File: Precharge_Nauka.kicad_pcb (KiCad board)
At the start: 2 copper layers, 80 parts, among them Q1 2N7002, Q2 C2M0280120D, Q3 C2M0280120D, Q4 C2M0280120D, Q5 C2M0280120D, U1 LM2903, U2 LMV321IDBVR, U3 74LVC1G08, U4 LMV321IDBVR

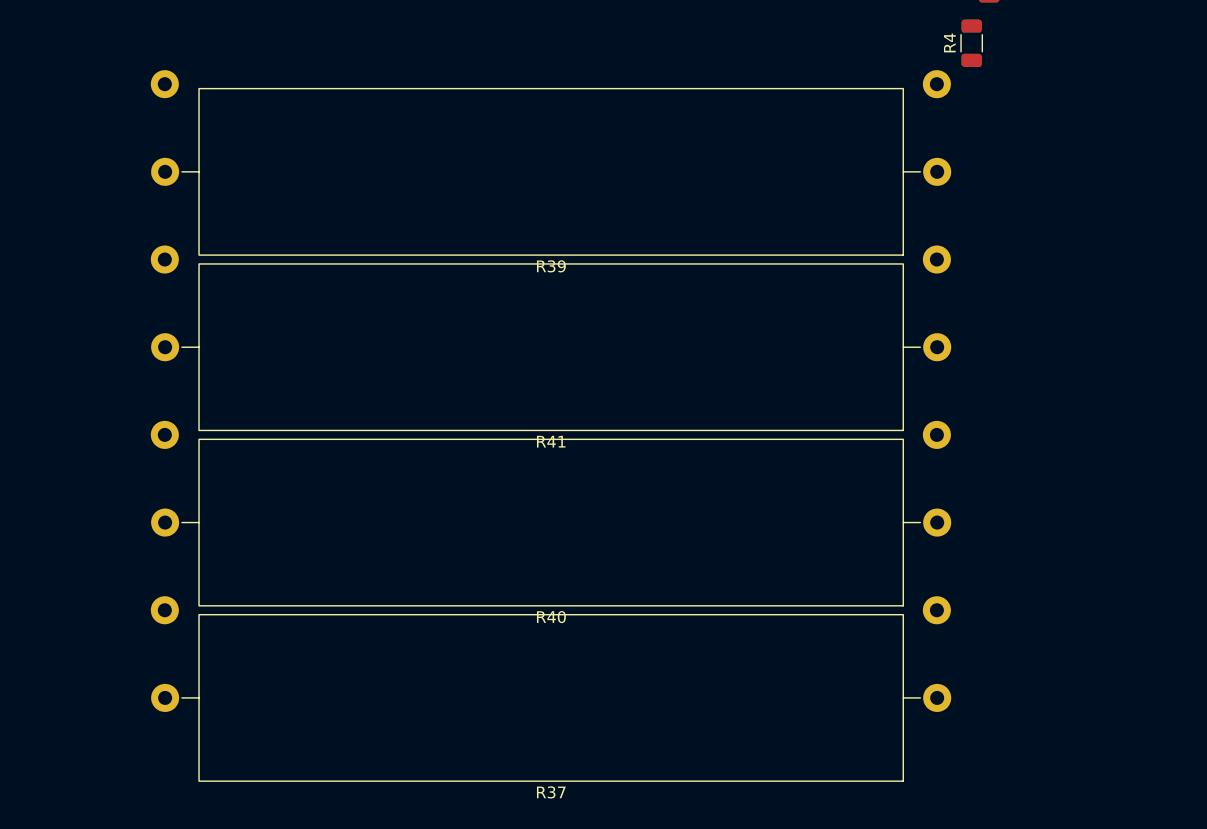
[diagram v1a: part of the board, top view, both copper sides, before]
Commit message: VER1.0: заменил цементные на 2512 резисторы
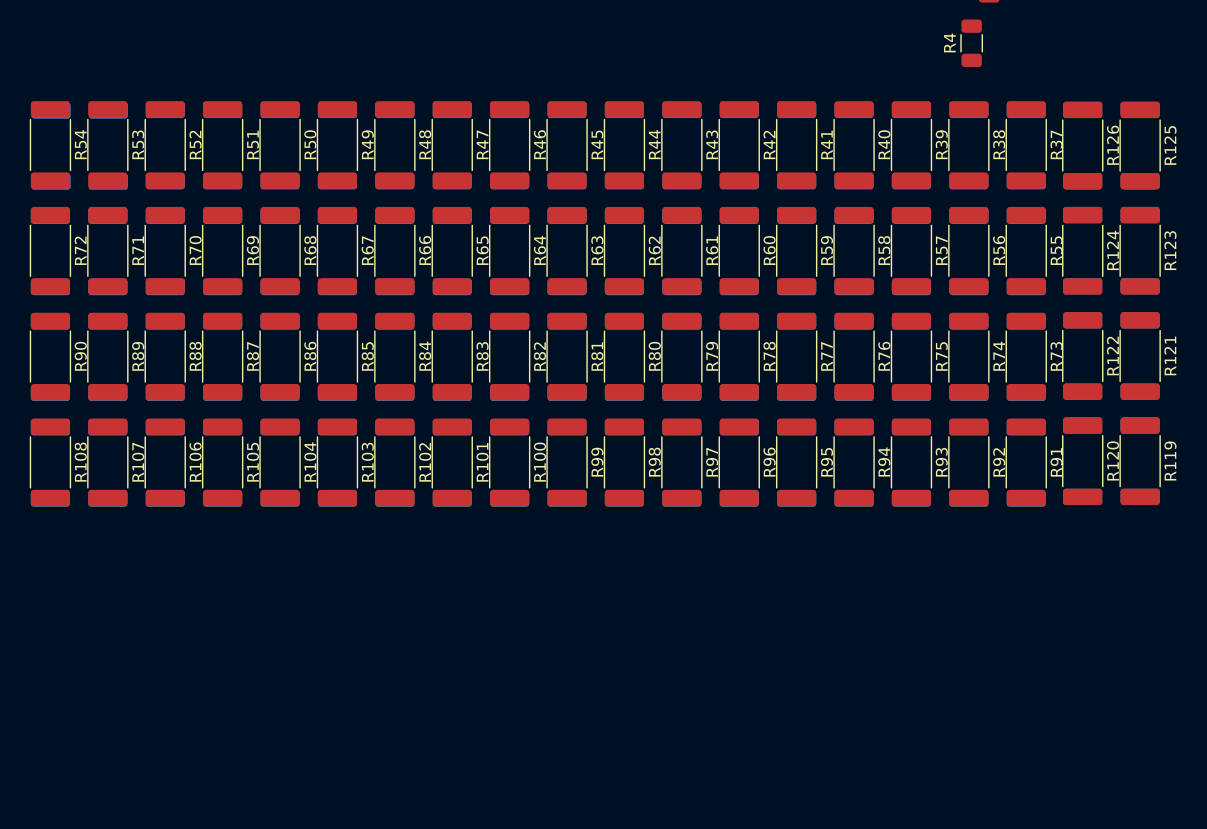
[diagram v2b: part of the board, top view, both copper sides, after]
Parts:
- added R100: 15, Resistor_SMD:R_2512_6332Metric_Pad1.40x3.35mm_HandSolder, F.Cu at (182.5, 224.6)
- added R101: 15, Resistor_SMD:R_2512_6332Metric_Pad1.40x3.35mm_HandSolder, F.Cu at (177.6, 224.6)
- added R102: 15, Resistor_SMD:R_2512_6332Metric_Pad1.40x3.35mm_HandSolder, F.Cu at (172.7, 224.6)
- added R103: 15, Resistor_SMD:R_2512_6332Metric_Pad1.40x3.35mm_HandSolder, F.Cu at (167.8, 224.6)
- added R104: 15, Resistor_SMD:R_2512_6332Metric_Pad1.40x3.35mm_HandSolder, F.Cu at (162.8, 224.6)
- added R105: 15, Resistor_SMD:R_2512_6332Metric_Pad1.40x3.35mm_HandSolder, F.Cu at (157.9, 224.6)
- added R106: 15, Resistor_SMD:R_2512_6332Metric_Pad1.40x3.35mm_HandSolder, F.Cu at (153.0, 224.6)
- added R107: 15, Resistor_SMD:R_2512_6332Metric_Pad1.40x3.35mm_HandSolder, F.Cu at (148.1, 224.6)
- added R108: 15, Resistor_SMD:R_2512_6332Metric_Pad1.40x3.35mm_HandSolder, F.Cu at (143.2, 224.6)
- added R109: 15, Resistor_SMD:R_2512_6332Metric_Pad1.40x3.35mm_HandSolder, B.Cu at (148.2, 197.6)
- added R110: 15, Resistor_SMD:R_2512_6332Metric_Pad1.40x3.35mm_HandSolder, B.Cu at (143.2, 197.6)
- added R111: 15, Resistor_SMD:R_2512_6332Metric_Pad1.40x3.35mm_HandSolder, B.Cu at (236.4, 197.5)
- added R112: 15, Resistor_SMD:R_2512_6332Metric_Pad1.40x3.35mm_HandSolder, B.Cu at (231.5, 197.5)
- added R113: 15, Resistor_SMD:R_2512_6332Metric_Pad1.40x3.35mm_HandSolder, B.Cu at (236.4, 206.5)
- added R114: 15, Resistor_SMD:R_2512_6332Metric_Pad1.40x3.35mm_HandSolder, B.Cu at (231.5, 206.5)
- added R115: 15, Resistor_SMD:R_2512_6332Metric_Pad1.40x3.35mm_HandSolder, B.Cu at (236.4, 215.5)
- added R116: 15, Resistor_SMD:R_2512_6332Metric_Pad1.40x3.35mm_HandSolder, B.Cu at (231.5, 215.5)
- added R117: 15, Resistor_SMD:R_2512_6332Metric_Pad1.40x3.35mm_HandSolder, B.Cu at (236.4, 224.5)
- added R118: 15, Resistor_SMD:R_2512_6332Metric_Pad1.40x3.35mm_HandSolder, B.Cu at (231.5, 224.5)
- added R119: 15, Resistor_SMD:R_2512_6332Metric_Pad1.40x3.35mm_HandSolder, F.Cu at (236.4, 224.5)
- added R120: 15, Resistor_SMD:R_2512_6332Metric_Pad1.40x3.35mm_HandSolder, F.Cu at (231.5, 224.5)
- added R121: 15, Resistor_SMD:R_2512_6332Metric_Pad1.40x3.35mm_HandSolder, F.Cu at (236.4, 215.5)
- added R122: 15, Resistor_SMD:R_2512_6332Metric_Pad1.40x3.35mm_HandSolder, F.Cu at (231.5, 215.5)
- added R123: 15, Resistor_SMD:R_2512_6332Metric_Pad1.40x3.35mm_HandSolder, F.Cu at (236.4, 206.5)
- added R124: 15, Resistor_SMD:R_2512_6332Metric_Pad1.40x3.35mm_HandSolder, F.Cu at (231.5, 206.5)
- added R125: 15, Resistor_SMD:R_2512_6332Metric_Pad1.40x3.35mm_HandSolder, F.Cu at (236.4, 197.5)
- added R126: 15, Resistor_SMD:R_2512_6332Metric_Pad1.40x3.35mm_HandSolder, F.Cu at (231.5, 197.5)
- added R127: 15, Resistor_SMD:R_2512_6332Metric_Pad1.40x3.35mm_HandSolder, B.Cu at (226.7, 224.7)
- added R128: 15, Resistor_SMD:R_2512_6332Metric_Pad1.40x3.35mm_HandSolder, B.Cu at (221.8, 224.7)
- added R129: 15, Resistor_SMD:R_2512_6332Metric_Pad1.40x3.35mm_HandSolder, B.Cu at (216.8, 224.7)
- added R130: 15, Resistor_SMD:R_2512_6332Metric_Pad1.40x3.35mm_HandSolder, B.Cu at (211.9, 224.7)
- added R131: 15, Resistor_SMD:R_2512_6332Metric_Pad1.40x3.35mm_HandSolder, B.Cu at (207.0, 224.7)
- added R132: 15, Resistor_SMD:R_2512_6332Metric_Pad1.40x3.35mm_HandSolder, B.Cu at (202.1, 224.7)
- added R133: 15, Resistor_SMD:R_2512_6332Metric_Pad1.40x3.35mm_HandSolder, B.Cu at (197.2, 224.7)
- added R134: 15, Resistor_SMD:R_2512_6332Metric_Pad1.40x3.35mm_HandSolder, B.Cu at (192.3, 224.7)
- added R135: 15, Resistor_SMD:R_2512_6332Metric_Pad1.40x3.35mm_HandSolder, B.Cu at (187.4, 224.7)
- added R136: 15, Resistor_SMD:R_2512_6332Metric_Pad1.40x3.35mm_HandSolder, B.Cu at (182.5, 224.7)
- added R137: 15, Resistor_SMD:R_2512_6332Metric_Pad1.40x3.35mm_HandSolder, B.Cu at (177.6, 224.7)
- added R138: 15, Resistor_SMD:R_2512_6332Metric_Pad1.40x3.35mm_HandSolder, B.Cu at (172.7, 224.7)
- added R139: 15, Resistor_SMD:R_2512_6332Metric_Pad1.40x3.35mm_HandSolder, B.Cu at (167.8, 224.7)
- added R140: 15, Resistor_SMD:R_2512_6332Metric_Pad1.40x3.35mm_HandSolder, B.Cu at (162.8, 224.7)
- added R141: 15, Resistor_SMD:R_2512_6332Metric_Pad1.40x3.35mm_HandSolder, B.Cu at (157.9, 224.7)
- added R142: 15, Resistor_SMD:R_2512_6332Metric_Pad1.40x3.35mm_HandSolder, B.Cu at (153.0, 224.7)
- added R143: 15, Resistor_SMD:R_2512_6332Metric_Pad1.40x3.35mm_HandSolder, B.Cu at (148.1, 224.7)
- added R144: 15, Resistor_SMD:R_2512_6332Metric_Pad1.40x3.35mm_HandSolder, B.Cu at (143.2, 224.7)
- added R145: 15, Resistor_SMD:R_2512_6332Metric_Pad1.40x3.35mm_HandSolder, B.Cu at (226.7, 215.6)
- added R146: 15, Resistor_SMD:R_2512_6332Metric_Pad1.40x3.35mm_HandSolder, B.Cu at (221.8, 215.6)
- added R147: 15, Resistor_SMD:R_2512_6332Metric_Pad1.40x3.35mm_HandSolder, B.Cu at (216.8, 215.6)
- added R148: 15, Resistor_SMD:R_2512_6332Metric_Pad1.40x3.35mm_HandSolder, B.Cu at (211.9, 215.6)
- added R149: 15, Resistor_SMD:R_2512_6332Metric_Pad1.40x3.35mm_HandSolder, B.Cu at (207.0, 215.6)
- added R150: 15, Resistor_SMD:R_2512_6332Metric_Pad1.40x3.35mm_HandSolder, B.Cu at (202.1, 215.6)
- added R151: 15, Resistor_SMD:R_2512_6332Metric_Pad1.40x3.35mm_HandSolder, B.Cu at (197.2, 215.6)
- added R152: 15, Resistor_SMD:R_2512_6332Metric_Pad1.40x3.35mm_HandSolder, B.Cu at (192.3, 215.6)
- added R153: 15, Resistor_SMD:R_2512_6332Metric_Pad1.40x3.35mm_HandSolder, B.Cu at (187.4, 215.6)
- added R154: 15, Resistor_SMD:R_2512_6332Metric_Pad1.40x3.35mm_HandSolder, B.Cu at (182.5, 215.6)
- added R155: 15, Resistor_SMD:R_2512_6332Metric_Pad1.40x3.35mm_HandSolder, B.Cu at (177.6, 215.6)
- added R156: 15, Resistor_SMD:R_2512_6332Metric_Pad1.40x3.35mm_HandSolder, B.Cu at (172.7, 215.6)
- added R157: 15, Resistor_SMD:R_2512_6332Metric_Pad1.40x3.35mm_HandSolder, B.Cu at (167.8, 215.6)
- added R158: 15, Resistor_SMD:R_2512_6332Metric_Pad1.40x3.35mm_HandSolder, B.Cu at (162.8, 215.6)
- added R159: 15, Resistor_SMD:R_2512_6332Metric_Pad1.40x3.35mm_HandSolder, B.Cu at (157.9, 215.6)
- added R160: 15, Resistor_SMD:R_2512_6332Metric_Pad1.40x3.35mm_HandSolder, B.Cu at (153.0, 215.6)
- added R161: 15, Resistor_SMD:R_2512_6332Metric_Pad1.40x3.35mm_HandSolder, B.Cu at (148.1, 215.6)
- added R162: 15, Resistor_SMD:R_2512_6332Metric_Pad1.40x3.35mm_HandSolder, B.Cu at (143.2, 215.6)
- added R163: 15, Resistor_SMD:R_2512_6332Metric_Pad1.40x3.35mm_HandSolder, B.Cu at (226.7, 206.6)
- added R164: 15, Resistor_SMD:R_2512_6332Metric_Pad1.40x3.35mm_HandSolder, B.Cu at (221.8, 206.6)
- added R165: 15, Resistor_SMD:R_2512_6332Metric_Pad1.40x3.35mm_HandSolder, B.Cu at (216.8, 206.6)
- added R166: 15, Resistor_SMD:R_2512_6332Metric_Pad1.40x3.35mm_HandSolder, B.Cu at (211.9, 206.6)
- added R167: 15, Resistor_SMD:R_2512_6332Metric_Pad1.40x3.35mm_HandSolder, B.Cu at (207.0, 206.6)
- added R168: 15, Resistor_SMD:R_2512_6332Metric_Pad1.40x3.35mm_HandSolder, B.Cu at (202.1, 206.6)
- added R169: 15, Resistor_SMD:R_2512_6332Metric_Pad1.40x3.35mm_HandSolder, B.Cu at (197.2, 206.6)
- added R170: 15, Resistor_SMD:R_2512_6332Metric_Pad1.40x3.35mm_HandSolder, B.Cu at (192.3, 206.6)
- added R171: 15, Resistor_SMD:R_2512_6332Metric_Pad1.40x3.35mm_HandSolder, B.Cu at (187.4, 206.6)
- added R172: 15, Resistor_SMD:R_2512_6332Metric_Pad1.40x3.35mm_HandSolder, B.Cu at (182.5, 206.6)
- added R173: 15, Resistor_SMD:R_2512_6332Metric_Pad1.40x3.35mm_HandSolder, B.Cu at (177.6, 206.6)
- added R174: 15, Resistor_SMD:R_2512_6332Metric_Pad1.40x3.35mm_HandSolder, B.Cu at (172.7, 206.6)
- added R175: 15, Resistor_SMD:R_2512_6332Metric_Pad1.40x3.35mm_HandSolder, B.Cu at (167.8, 206.6)
- added R176: 15, Resistor_SMD:R_2512_6332Metric_Pad1.40x3.35mm_HandSolder, B.Cu at (162.8, 206.6)
- added R177: 15, Resistor_SMD:R_2512_6332Metric_Pad1.40x3.35mm_HandSolder, B.Cu at (157.9, 206.6)
- added R178: 15, Resistor_SMD:R_2512_6332Metric_Pad1.40x3.35mm_HandSolder, B.Cu at (153.0, 206.6)
- added R179: 15, Resistor_SMD:R_2512_6332Metric_Pad1.40x3.35mm_HandSolder, B.Cu at (148.1, 206.6)
- added R180: 15, Resistor_SMD:R_2512_6332Metric_Pad1.40x3.35mm_HandSolder, B.Cu at (143.2, 206.6)
- added R181: 15, Resistor_SMD:R_2512_6332Metric_Pad1.40x3.35mm_HandSolder, B.Cu at (226.7, 197.5)
- added R182: 15, Resistor_SMD:R_2512_6332Metric_Pad1.40x3.35mm_HandSolder, B.Cu at (221.8, 197.5)
- added R183: 15, Resistor_SMD:R_2512_6332Metric_Pad1.40x3.35mm_HandSolder, B.Cu at (216.8, 197.5)
- added R184: 15, Resistor_SMD:R_2512_6332Metric_Pad1.40x3.35mm_HandSolder, B.Cu at (211.9, 197.5)
- added R185: 15, Resistor_SMD:R_2512_6332Metric_Pad1.40x3.35mm_HandSolder, B.Cu at (207.0, 197.5)
- added R186: 15, Resistor_SMD:R_2512_6332Metric_Pad1.40x3.35mm_HandSolder, B.Cu at (202.1, 197.5)
- added R187: 15, Resistor_SMD:R_2512_6332Metric_Pad1.40x3.35mm_HandSolder, B.Cu at (197.2, 197.5)
- added R188: 15, Resistor_SMD:R_2512_6332Metric_Pad1.40x3.35mm_HandSolder, B.Cu at (192.3, 197.5)
- added R189: 15, Resistor_SMD:R_2512_6332Metric_Pad1.40x3.35mm_HandSolder, B.Cu at (187.4, 197.5)
- added R190: 15, Resistor_SMD:R_2512_6332Metric_Pad1.40x3.35mm_HandSolder, B.Cu at (182.5, 197.5)
- added R191: 15, Resistor_SMD:R_2512_6332Metric_Pad1.40x3.35mm_HandSolder, B.Cu at (177.6, 197.5)
- added R192: 15, Resistor_SMD:R_2512_6332Metric_Pad1.40x3.35mm_HandSolder, B.Cu at (172.7, 197.5)
- added R193: 15, Resistor_SMD:R_2512_6332Metric_Pad1.40x3.35mm_HandSolder, B.Cu at (167.8, 197.5)
- added R194: 15, Resistor_SMD:R_2512_6332Metric_Pad1.40x3.35mm_HandSolder, B.Cu at (162.8, 197.5)
- added R195: 15, Resistor_SMD:R_2512_6332Metric_Pad1.40x3.35mm_HandSolder, B.Cu at (157.9, 197.5)
- added R196: 15, Resistor_SMD:R_2512_6332Metric_Pad1.40x3.35mm_HandSolder, B.Cu at (153.0, 197.5)
- added R45: 15, Resistor_SMD:R_2512_6332Metric_Pad1.40x3.35mm_HandSolder, F.Cu at (187.4, 197.4)
- added R46: 15, Resistor_SMD:R_2512_6332Metric_Pad1.40x3.35mm_HandSolder, F.Cu at (182.5, 197.4)
- added R47: 15, Resistor_SMD:R_2512_6332Metric_Pad1.40x3.35mm_HandSolder, F.Cu at (177.6, 197.4)
- added R48: 15, Resistor_SMD:R_2512_6332Metric_Pad1.40x3.35mm_HandSolder, F.Cu at (172.7, 197.4)
- added R49: 15, Resistor_SMD:R_2512_6332Metric_Pad1.40x3.35mm_HandSolder, F.Cu at (167.8, 197.4)
- added R50: 15, Resistor_SMD:R_2512_6332Metric_Pad1.40x3.35mm_HandSolder, F.Cu at (162.8, 197.4)
- added R51: 15, Resistor_SMD:R_2512_6332Metric_Pad1.40x3.35mm_HandSolder, F.Cu at (157.9, 197.4)
- added R52: 15, Resistor_SMD:R_2512_6332Metric_Pad1.40x3.35mm_HandSolder, F.Cu at (153.0, 197.4)
- added R53: 15, Resistor_SMD:R_2512_6332Metric_Pad1.40x3.35mm_HandSolder, F.Cu at (148.1, 197.4)
- added R54: 15, Resistor_SMD:R_2512_6332Metric_Pad1.40x3.35mm_HandSolder, F.Cu at (143.2, 197.4)
- added R55: 15, Resistor_SMD:R_2512_6332Metric_Pad1.40x3.35mm_HandSolder, F.Cu at (226.7, 206.5)
- added R56: 15, Resistor_SMD:R_2512_6332Metric_Pad1.40x3.35mm_HandSolder, F.Cu at (221.8, 206.5)
- added R57: 15, Resistor_SMD:R_2512_6332Metric_Pad1.40x3.35mm_HandSolder, F.Cu at (216.8, 206.5)
- added R58: 15, Resistor_SMD:R_2512_6332Metric_Pad1.40x3.35mm_HandSolder, F.Cu at (211.9, 206.5)
- added R59: 15, Resistor_SMD:R_2512_6332Metric_Pad1.40x3.35mm_HandSolder, F.Cu at (207.0, 206.5)
- added R60: 15, Resistor_SMD:R_2512_6332Metric_Pad1.40x3.35mm_HandSolder, F.Cu at (202.1, 206.5)
- added R61: 15, Resistor_SMD:R_2512_6332Metric_Pad1.40x3.35mm_HandSolder, F.Cu at (197.2, 206.5)
- added R62: 15, Resistor_SMD:R_2512_6332Metric_Pad1.40x3.35mm_HandSolder, F.Cu at (192.3, 206.5)
- added R63: 15, Resistor_SMD:R_2512_6332Metric_Pad1.40x3.35mm_HandSolder, F.Cu at (187.4, 206.5)
- added R64: 15, Resistor_SMD:R_2512_6332Metric_Pad1.40x3.35mm_HandSolder, F.Cu at (182.5, 206.5)
- added R65: 15, Resistor_SMD:R_2512_6332Metric_Pad1.40x3.35mm_HandSolder, F.Cu at (177.6, 206.5)
- added R66: 15, Resistor_SMD:R_2512_6332Metric_Pad1.40x3.35mm_HandSolder, F.Cu at (172.7, 206.5)
- added R67: 15, Resistor_SMD:R_2512_6332Metric_Pad1.40x3.35mm_HandSolder, F.Cu at (167.8, 206.5)
- added R68: 15, Resistor_SMD:R_2512_6332Metric_Pad1.40x3.35mm_HandSolder, F.Cu at (162.8, 206.5)
- added R69: 15, Resistor_SMD:R_2512_6332Metric_Pad1.40x3.35mm_HandSolder, F.Cu at (157.9, 206.5)
- added R70: 15, Resistor_SMD:R_2512_6332Metric_Pad1.40x3.35mm_HandSolder, F.Cu at (153.0, 206.5)
- added R71: 15, Resistor_SMD:R_2512_6332Metric_Pad1.40x3.35mm_HandSolder, F.Cu at (148.1, 206.5)
- added R72: 15, Resistor_SMD:R_2512_6332Metric_Pad1.40x3.35mm_HandSolder, F.Cu at (143.2, 206.5)
- added R73: 15, Resistor_SMD:R_2512_6332Metric_Pad1.40x3.35mm_HandSolder, F.Cu at (226.7, 215.6)
- added R74: 15, Resistor_SMD:R_2512_6332Metric_Pad1.40x3.35mm_HandSolder, F.Cu at (221.8, 215.6)
- added R75: 15, Resistor_SMD:R_2512_6332Metric_Pad1.40x3.35mm_HandSolder, F.Cu at (216.8, 215.6)
- added R76: 15, Resistor_SMD:R_2512_6332Metric_Pad1.40x3.35mm_HandSolder, F.Cu at (211.9, 215.6)
- added R77: 15, Resistor_SMD:R_2512_6332Metric_Pad1.40x3.35mm_HandSolder, F.Cu at (207.0, 215.6)
- added R78: 15, Resistor_SMD:R_2512_6332Metric_Pad1.40x3.35mm_HandSolder, F.Cu at (202.1, 215.6)
- added R79: 15, Resistor_SMD:R_2512_6332Metric_Pad1.40x3.35mm_HandSolder, F.Cu at (197.2, 215.6)
- added R80: 15, Resistor_SMD:R_2512_6332Metric_Pad1.40x3.35mm_HandSolder, F.Cu at (192.3, 215.6)
- added R81: 15, Resistor_SMD:R_2512_6332Metric_Pad1.40x3.35mm_HandSolder, F.Cu at (187.4, 215.6)
- added R82: 15, Resistor_SMD:R_2512_6332Metric_Pad1.40x3.35mm_HandSolder, F.Cu at (182.5, 215.6)
- added R83: 15, Resistor_SMD:R_2512_6332Metric_Pad1.40x3.35mm_HandSolder, F.Cu at (177.6, 215.6)
- added R84: 15, Resistor_SMD:R_2512_6332Metric_Pad1.40x3.35mm_HandSolder, F.Cu at (172.7, 215.6)
- added R85: 15, Resistor_SMD:R_2512_6332Metric_Pad1.40x3.35mm_HandSolder, F.Cu at (167.8, 215.6)
- added R86: 15, Resistor_SMD:R_2512_6332Metric_Pad1.40x3.35mm_HandSolder, F.Cu at (162.8, 215.6)
- added R87: 15, Resistor_SMD:R_2512_6332Metric_Pad1.40x3.35mm_HandSolder, F.Cu at (157.9, 215.6)
- added R88: 15, Resistor_SMD:R_2512_6332Metric_Pad1.40x3.35mm_HandSolder, F.Cu at (153.0, 215.6)
- added R89: 15, Resistor_SMD:R_2512_6332Metric_Pad1.40x3.35mm_HandSolder, F.Cu at (148.1, 215.6)
- added R90: 15, Resistor_SMD:R_2512_6332Metric_Pad1.40x3.35mm_HandSolder, F.Cu at (143.2, 215.6)
- added R91: 15, Resistor_SMD:R_2512_6332Metric_Pad1.40x3.35mm_HandSolder, F.Cu at (226.7, 224.6)
- added R92: 15, Resistor_SMD:R_2512_6332Metric_Pad1.40x3.35mm_HandSolder, F.Cu at (221.8, 224.6)
- added R93: 15, Resistor_SMD:R_2512_6332Metric_Pad1.40x3.35mm_HandSolder, F.Cu at (216.8, 224.6)
- added R94: 15, Resistor_SMD:R_2512_6332Metric_Pad1.40x3.35mm_HandSolder, F.Cu at (211.9, 224.6)
- added R95: 15, Resistor_SMD:R_2512_6332Metric_Pad1.40x3.35mm_HandSolder, F.Cu at (207.0, 224.6)
- added R96: 15, Resistor_SMD:R_2512_6332Metric_Pad1.40x3.35mm_HandSolder, F.Cu at (202.1, 224.6)
- added R97: 15, Resistor_SMD:R_2512_6332Metric_Pad1.40x3.35mm_HandSolder, F.Cu at (197.2, 224.6)
- added R98: 15, Resistor_SMD:R_2512_6332Metric_Pad1.40x3.35mm_HandSolder, F.Cu at (192.3, 224.6)
- added R99: 15, Resistor_SMD:R_2512_6332Metric_Pad1.40x3.35mm_HandSolder, F.Cu at (187.4, 224.6)
- C10: value 1u -> 100n
- R37, R39, R40, R41: value 10k -> 15; footprint Resistor_THT:R_Axial_Power_L60.0mm_W14.0mm_P66.04mm -> Resistor_SMD:R_2512_6332Metric_Pad1.40x3.35mm_HandSolder
- R38, R42, R43, R44: value 10k -> 15; footprint Resistor_THT:R_Axial_Power_L60.0mm_W14.0mm_P66.04mm -> Resistor_SMD:R_2512_6332Metric_Pad1.40x3.35mm_HandSolder; moved to F.Cu
- moved R37 47.9 mm to (226.7, 197.4), turned to -90 degrees
- moved R38 39.9 mm to (221.8, 197.4), turned to -90 degrees
- moved R44 36.5 mm to (192.3, 197.4), turned to -90 degrees
- moved R40 33.1 mm to (211.9, 197.4), turned to -90 degrees
- moved R43 22.4 mm to (197.2, 197.4), turned to -90 degrees
- moved R41 21.1 mm to (207.0, 197.4), turned to -90 degrees
- moved R42 19.5 mm to (202.1, 197.4), turned to -90 degrees
- moved R39 3.18 mm to (216.8, 197.4), turned to -90 degrees
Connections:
- R37 pad 1: VDC_IN -> VDC_OUT
- R37 pad 2: VDC_OUT -> VDC_IN
- R38 pad 1: VDC_IN -> VDC_OUT
- R38 pad 2: VDC_OUT -> VDC_IN
- R39 pad 1: VDC_IN -> VDC_OUT
- R39 pad 2: VDC_OUT -> VDC_IN
- R40 pad 1: VDC_IN -> VDC_OUT
- R40 pad 2: VDC_OUT -> VDC_IN
- R41 pad 1: VDC_IN -> VDC_OUT
- R41 pad 2: VDC_OUT -> VDC_IN
- R42 pad 1: VDC_IN -> VDC_OUT
- R42 pad 2: VDC_OUT -> VDC_IN
- R43 pad 1: VDC_IN -> VDC_OUT
- R43 pad 2: VDC_OUT -> VDC_IN
- R44 pad 1: VDC_IN -> VDC_OUT
- R44 pad 2: VDC_OUT -> VDC_IN

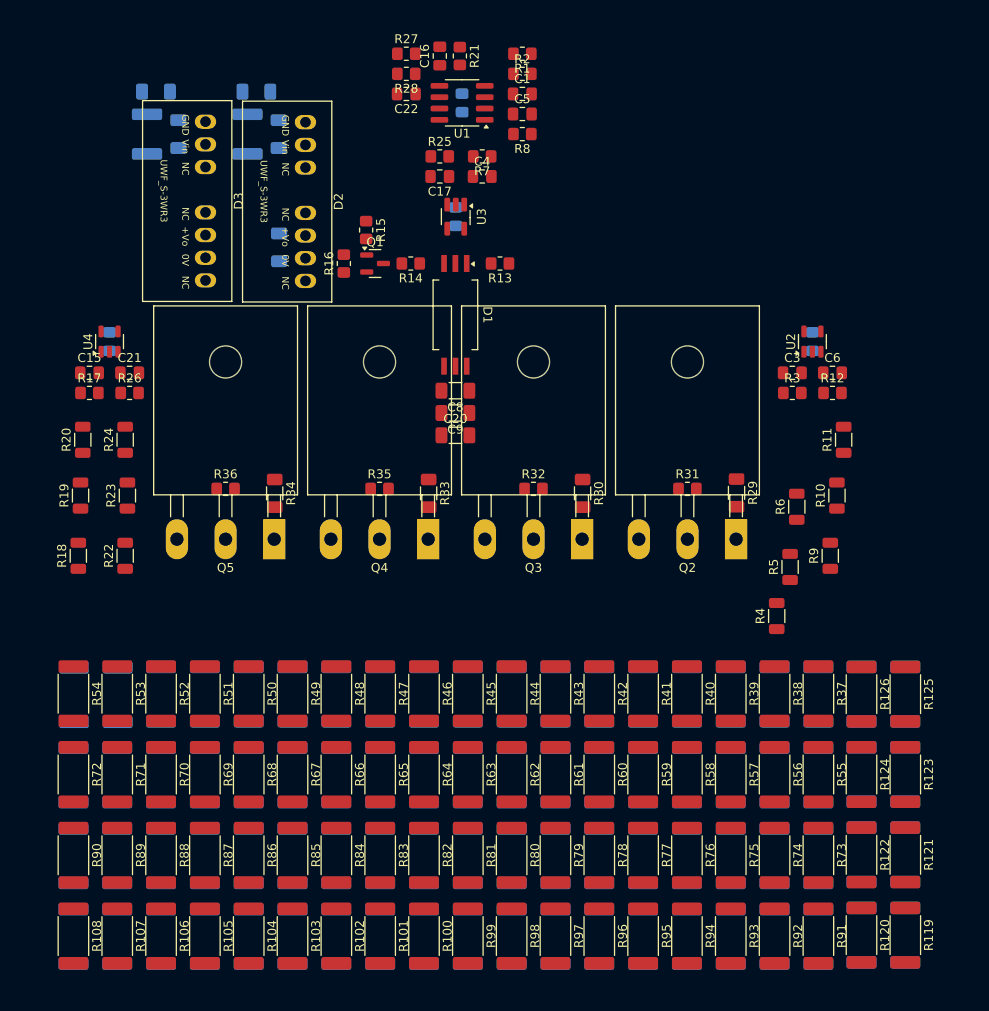
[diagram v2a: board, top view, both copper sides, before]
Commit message: VER1.0: надо проверить посадку новых транзисторов. Добавил обратную свзязь для компараторов
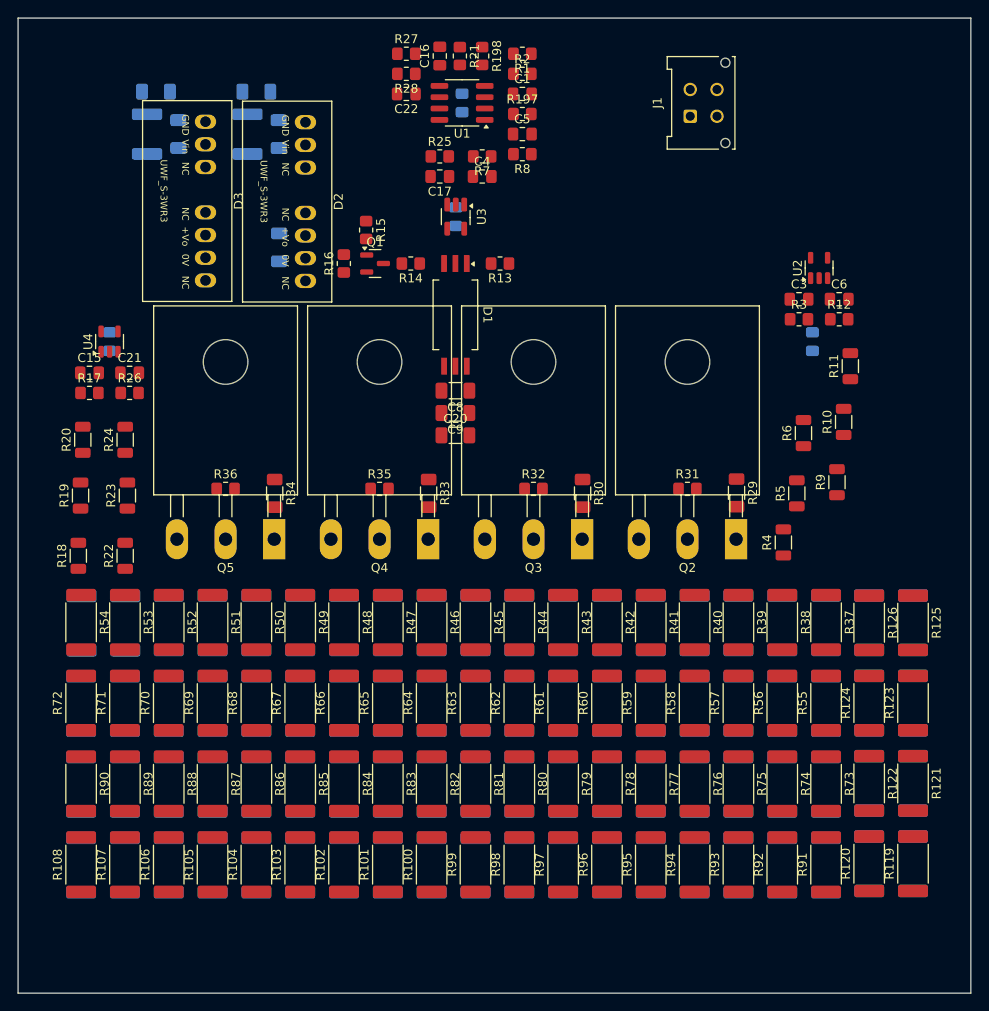
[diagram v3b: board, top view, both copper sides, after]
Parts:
- added J1: Conn_02x02_Top_Bottom, Connector_Molex:Molex_Micro-Fit_3.0_43045-0412_2x02_P3.00mm_Vertical, F.Cu at (212.3, 132.8)
- added R197: 10k, Resistor_SMD:R_0805_2012Metric_Pad1.20x1.40mm_HandSolder, F.Cu at (193.5, 132.5)
- added R198: 10k, Resistor_SMD:R_0805_2012Metric_Pad1.20x1.40mm_HandSolder, F.Cu at (189.0, 126.0)
- D1: value ~ -> NSI6801
- moved C3 8.28 mm to (224.5, 153.2)
- moved C6 8.28 mm to (229.0, 153.2)
- moved R10 8.28 mm to (229.5, 167.0)
- moved R11 8.28 mm to (230.2, 160.8)
- moved R12 8.28 mm to (229.0, 155.5)
- moved R3 8.28 mm to (224.5, 155.5)
- moved R4 8.28 mm to (222.8, 180.5)
- moved R5 8.28 mm to (224.2, 175.0)
- moved R6 8.28 mm to (225.0, 168.2)
- moved R9 8.28 mm to (228.8, 173.8)
- moved U2 8.28 mm to (226.8, 149.8)
- moved R100 8.05 mm to (183.3, 216.6), turned to 90 degrees
- moved R101 8.05 mm to (178.4, 216.6), turned to 90 degrees
- moved R102 8.05 mm to (173.5, 216.6), turned to 90 degrees
- moved R103 8.05 mm to (168.6, 216.6), turned to 90 degrees
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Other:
- board outline added: 106.8 x 109.2 mm

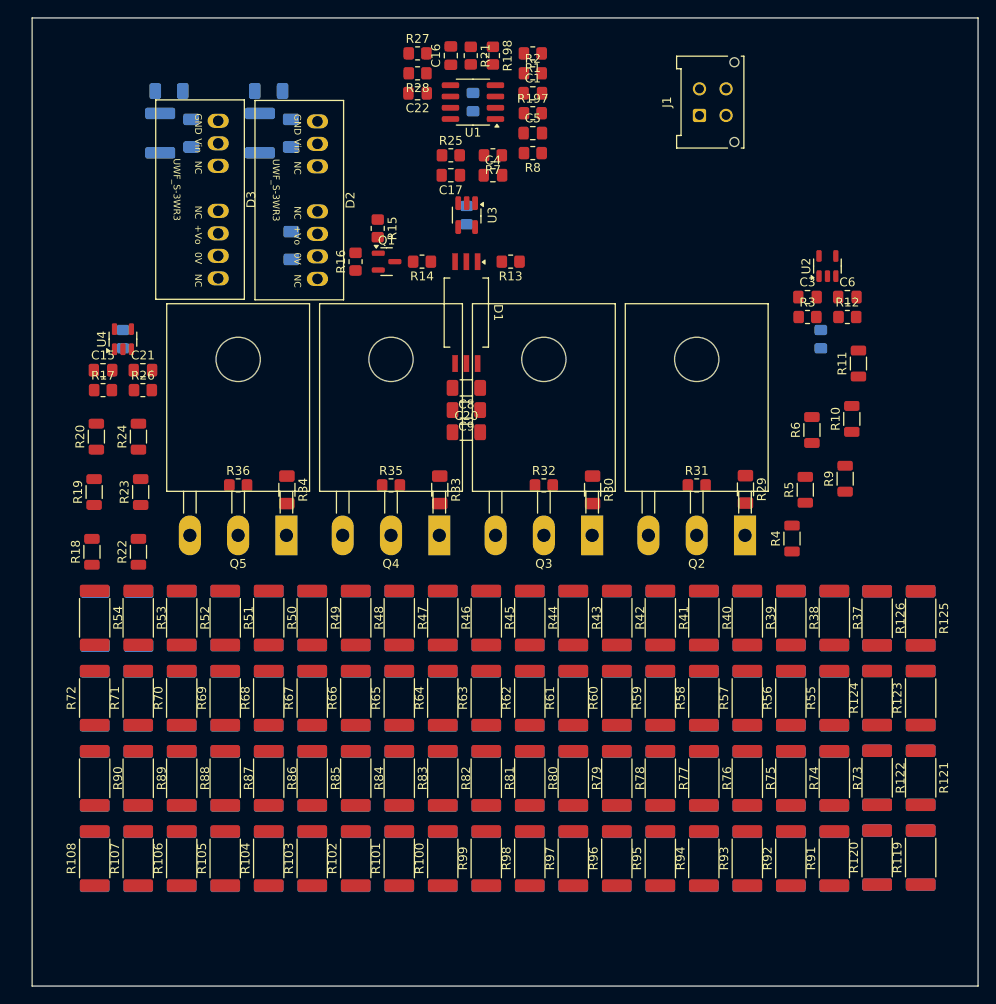
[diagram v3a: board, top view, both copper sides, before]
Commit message: VER1.0: добавил силовые стойки и развел силу
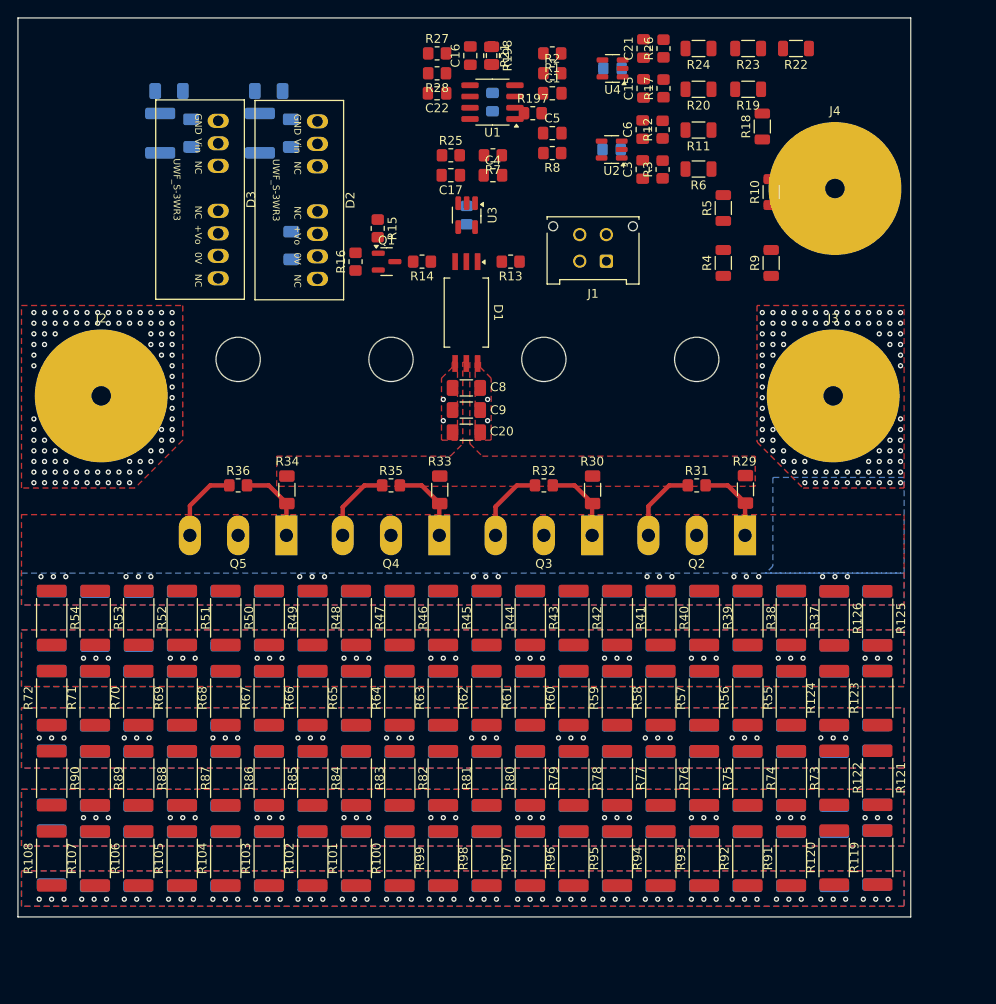
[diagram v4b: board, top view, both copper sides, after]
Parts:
- added J2: Conn_01x01, Connector_Power:SMD_15mm, F.Cu at (144.8, 164.4)
- added J3: Conn_01x01, Connector_Power:SMD_15mm, F.Cu at (227.4, 164.4)
- added J4: Conn_01x01, Connector_Power:SMD_15mm, F.Cu at (227.6, 141.0)
- moved R111 98.1 mm to (139.2, 189.5)
- moved R113 98.1 mm to (139.2, 198.5)
- moved R115 98.1 mm to (139.2, 207.5)
- moved R117 98.1 mm to (139.2, 216.5)
- moved R22 93.4 mm to (223.2, 125.2), turned to 180 degrees
- moved R18 89.6 mm to (219.4, 134.0)
- moved R19 86.7 mm to (217.8, 129.8), turned to 180 degrees
- moved R23 84.9 mm to (217.8, 125.2), turned to 180 degrees
- moved R20 78.4 mm to (212.2, 129.8), turned to 180 degrees
- moved R24 76.9 mm to (212.2, 125.2), turned to 180 degrees
- moved R17 71.8 mm to (208.2, 129.7), turned to 90 degrees
- moved R26 70.3 mm to (208.2, 125.2), turned to 90 degrees
- moved C15 68.8 mm to (206.0, 129.7), turned to 90 degrees
- moved C21 67.2 mm to (206.0, 125.2), turned to 90 degrees
- moved C14 63.1 mm to (202.5, 127.5), turned to 0 degrees
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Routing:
- net VCC: track 0.00 -> 46.4 mm, vias 0 -> 2
- net VDC_OUT: track 0.00 -> 43.8 mm, vias 0 -> 203
- net Net-(Q2-G): track 0.00 -> 8.99 mm
- net Net-(Q5-G): track 0.00 -> 8.96 mm
- net Net-(Q4-G): track 0.00 -> 8.96 mm
- net Net-(Q3-G): track 0.00 -> 8.96 mm
- net VDC_IN: vias 0 -> 150
- added copper zone on F.Cu, net Gate
- added copper zone on F.Cu, net VCC
- added copper zone on B.Cu, net VDC_IN
- added copper zone on F.Cu, net VDC_IN
- added copper zone on In2.Cu, net VDC_IN
- added copper zone on B.Cu, net VDC_OUT
- added copper zone on F.Cu, net VDC_OUT
- added copper zone on In1.Cu, net VDC_OUT
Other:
- board size 106.8 x 109.2 mm -> 100.8 x 101.4 mm
- copper layers 2 -> 4
